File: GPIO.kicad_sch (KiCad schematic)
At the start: 7 parts, among them J9 uPD446

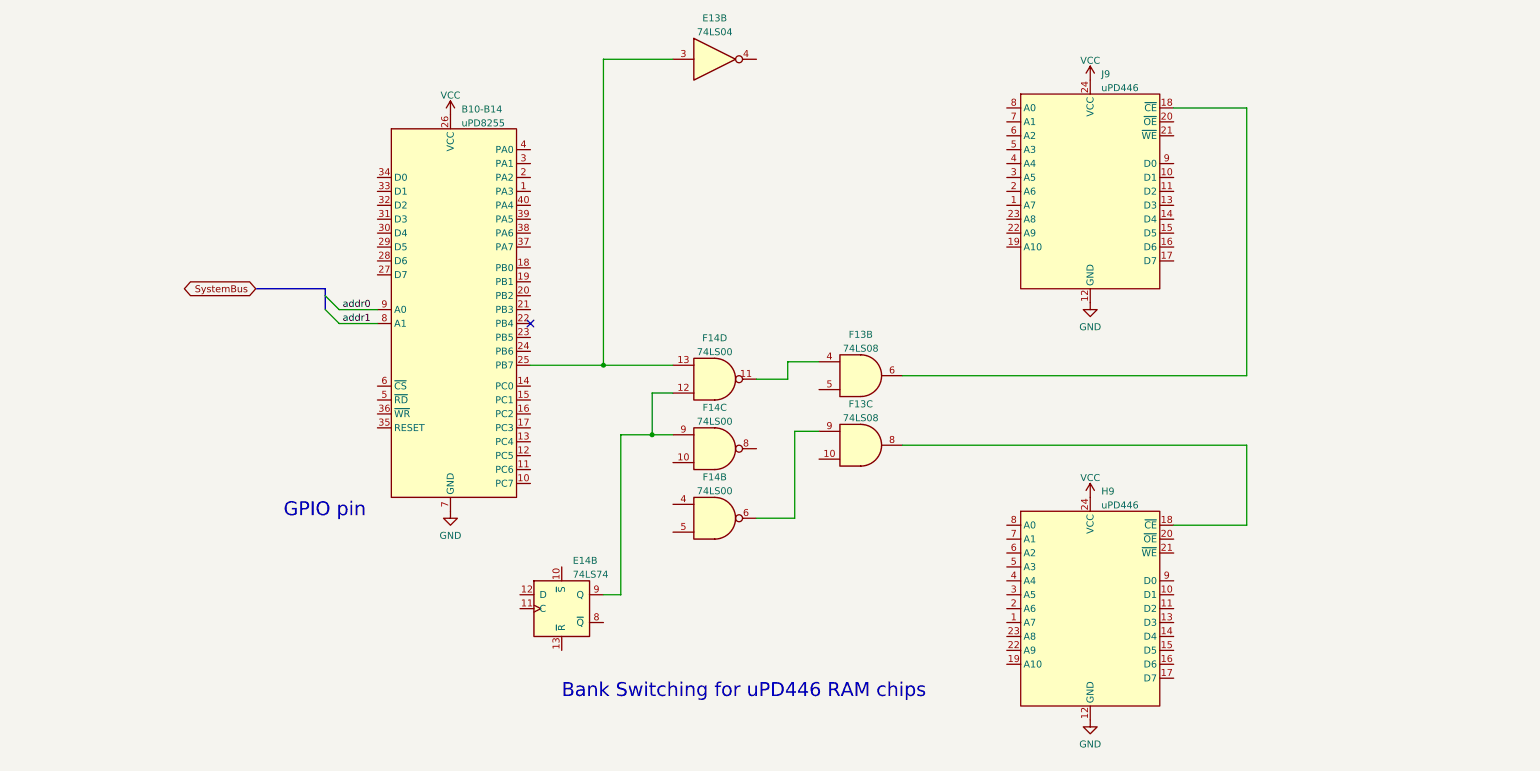
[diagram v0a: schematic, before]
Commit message: Some steps in bank switching and crtc circuits
- crtc pixel clock generator
- 2k ram, enabling logic (heavily incomplete)
- other 2k ram, annotation regarding data bus
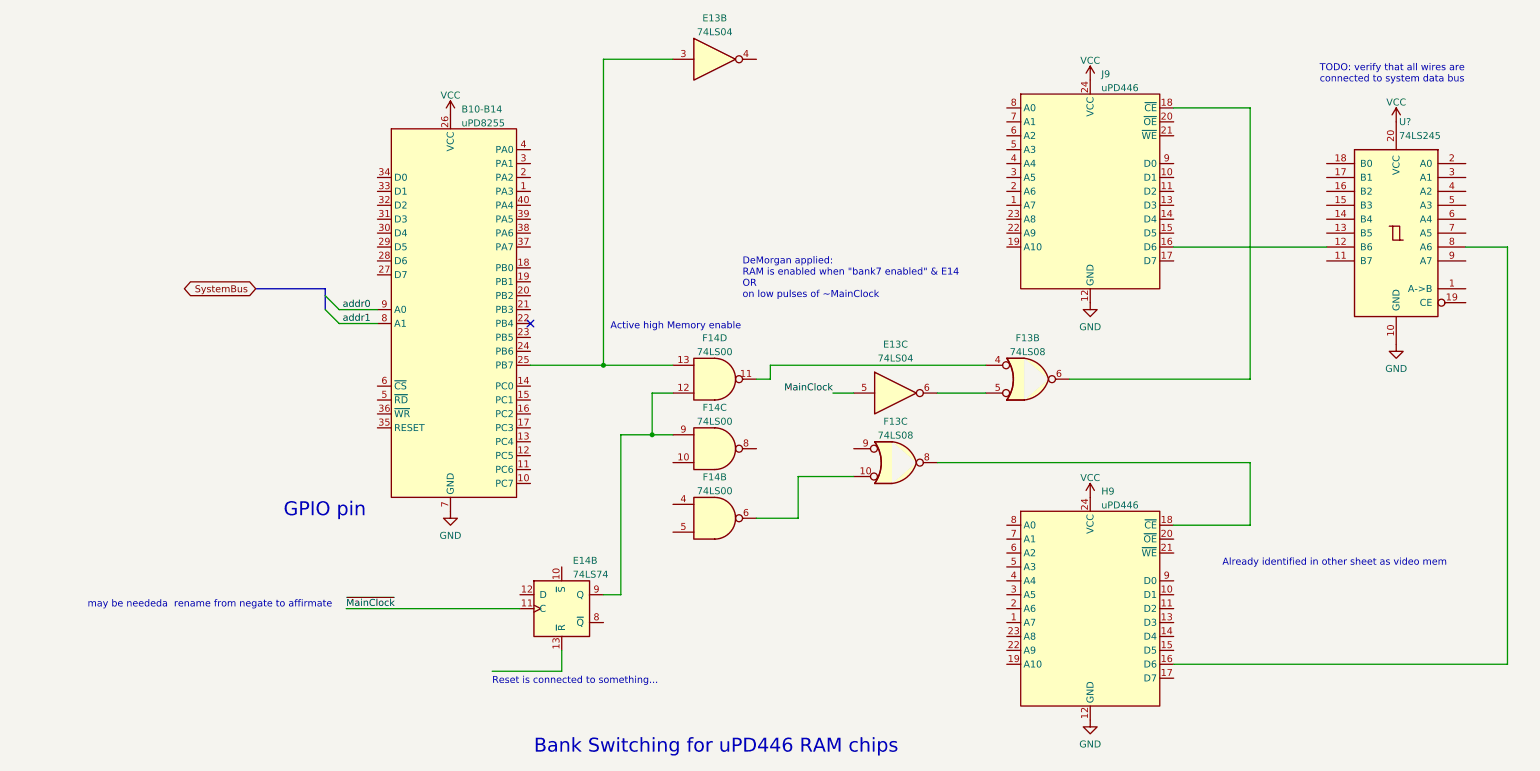
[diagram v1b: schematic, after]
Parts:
- added unit 3 of E13
- added U?: 74LS245, symbol 74xx:74LS245
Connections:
- net GND: now also U?.10 (GND)
- net VCC: now also U?.20 (VCC)
- net at F14.6: now also F13.10; no longer F13.9
- net ~{MainClock}: now reaches E14.11 (C)
- net at H9.16 (D6): now also U?.8 (A6)
- net at J9.16 (D6): now also U?.12 (B6)
- net at F13.5: now also E13.6
- new net MainClock: E13.5
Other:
- note added: "Active high Memory enable"
- note added: "Already identified in other sheet as video mem"
- note added: "DeMorgan applied: RAM is enabled when "bank7 enabled" & E14 OR on low pulses of ~MainClock"
- note added: "Reset is connected to something..."
- note added: "TODO: verify that all wires are connected to system data bus"
- note added: "may be neededa rename from negate to affirmate"

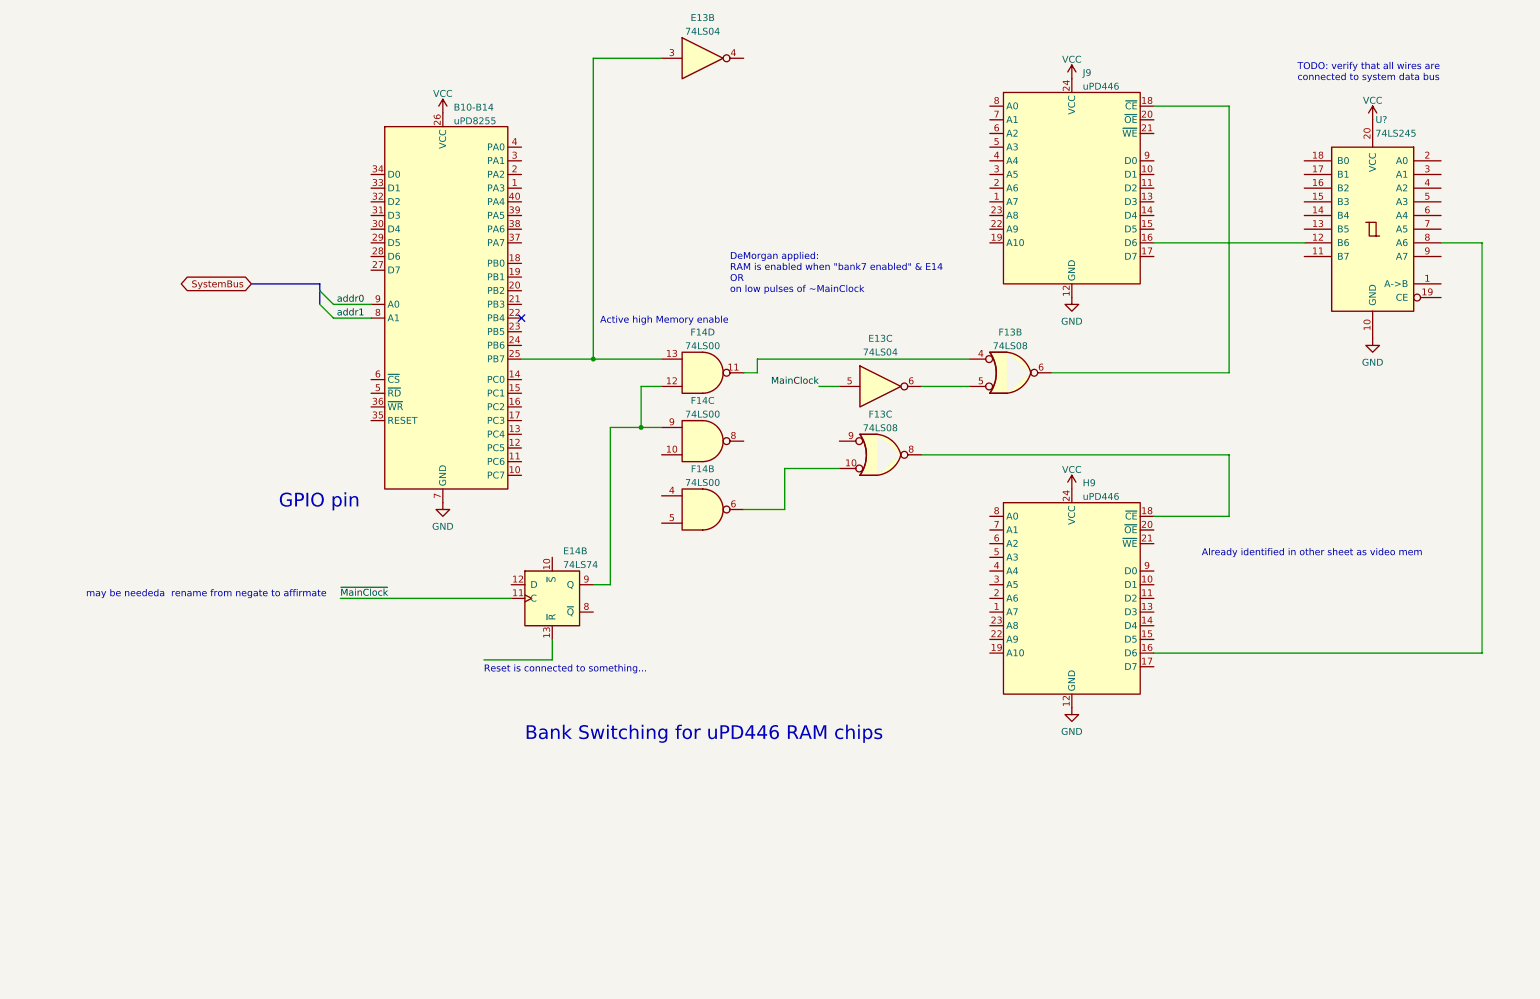
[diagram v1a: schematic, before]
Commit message: Video memory bus and connections to Z80
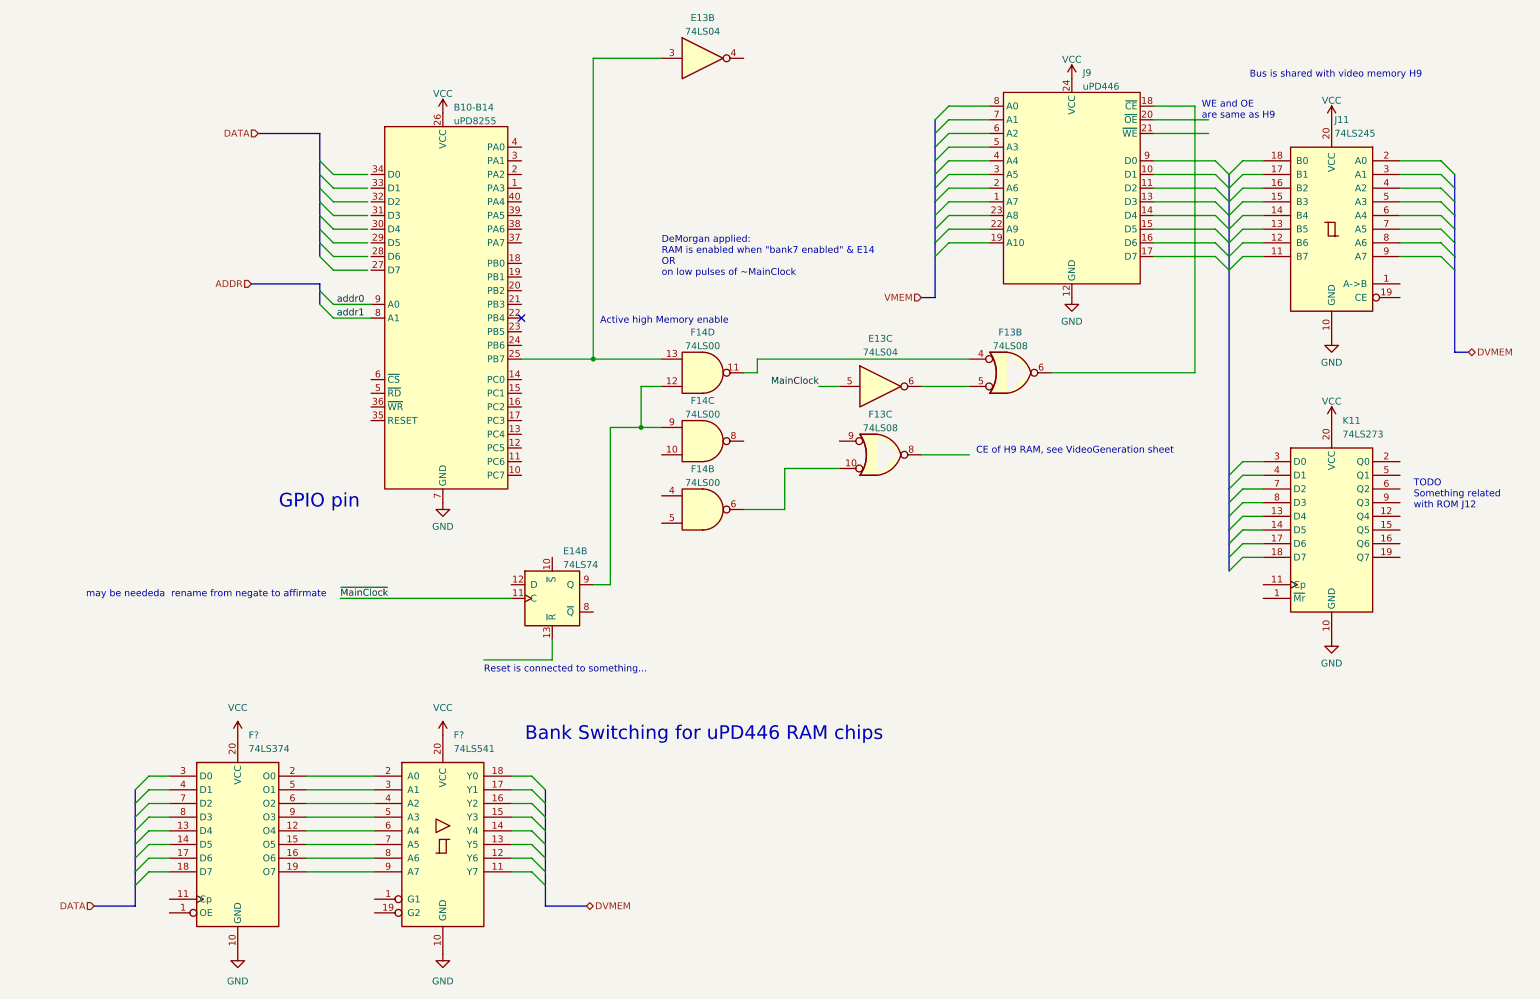
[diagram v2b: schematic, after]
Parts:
- removed H9: uPD446, symbol ceda:uPD446
- added F?: 74LS541, symbol 74xx:74LS541
- added F?: 74LS374, symbol 74xx:74LS374
- added K11: 74LS273, symbol 74xx:74LS273
- gave numbers to parts that had none: 1
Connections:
- net GND: now also F?.10 (GND), F?.10 (GND), K11.10 (GND)
- net VCC: now also F?.20 (VCC), F?.20 (VCC), K11.20 (VCC)
- net at J11.12 (B6): no longer J9.16 (D6)
- new net: F?.2 (A0), F?.2 (O0)
- new net: F?.3 (A1), F?.5 (O1)
- new net: F?.4 (A2), F?.6 (O2)
- new net: F?.5 (A3), F?.9 (O3)
- new net: F?.12 (O4), F?.6 (A4)
- new net: F?.15 (O5), F?.7 (A5)
- new net: F?.16 (O6), F?.8 (A6)
- new net: F?.19 (O7), F?.9 (A7)
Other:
- note added: "Bus is shared with video memory H9"
- note added: "CE of H9 RAM, see VideoGeneration sheet"
- note added: "TODO Something related with ROM J12"
- note added: "WE and OE are same as H9"
- note removed: "Already identified in other sheet as video mem"
- note removed: "TODO: verify that all wires are connected to system data bus"
- moved on the sheet: J11

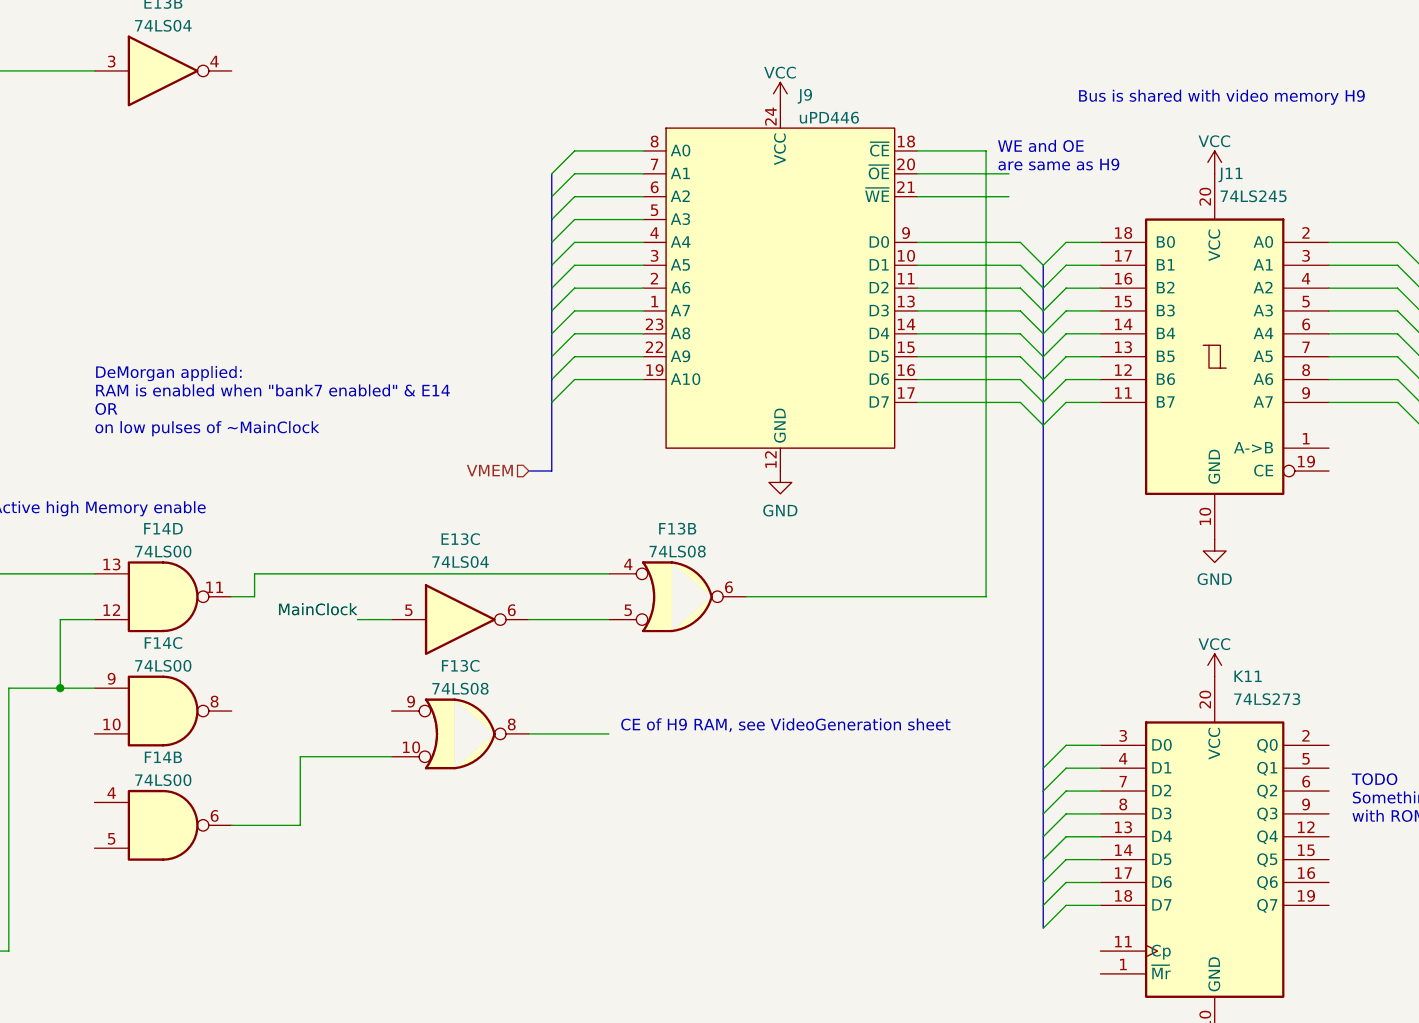
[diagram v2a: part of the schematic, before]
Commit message: Upgraded to kicad 7
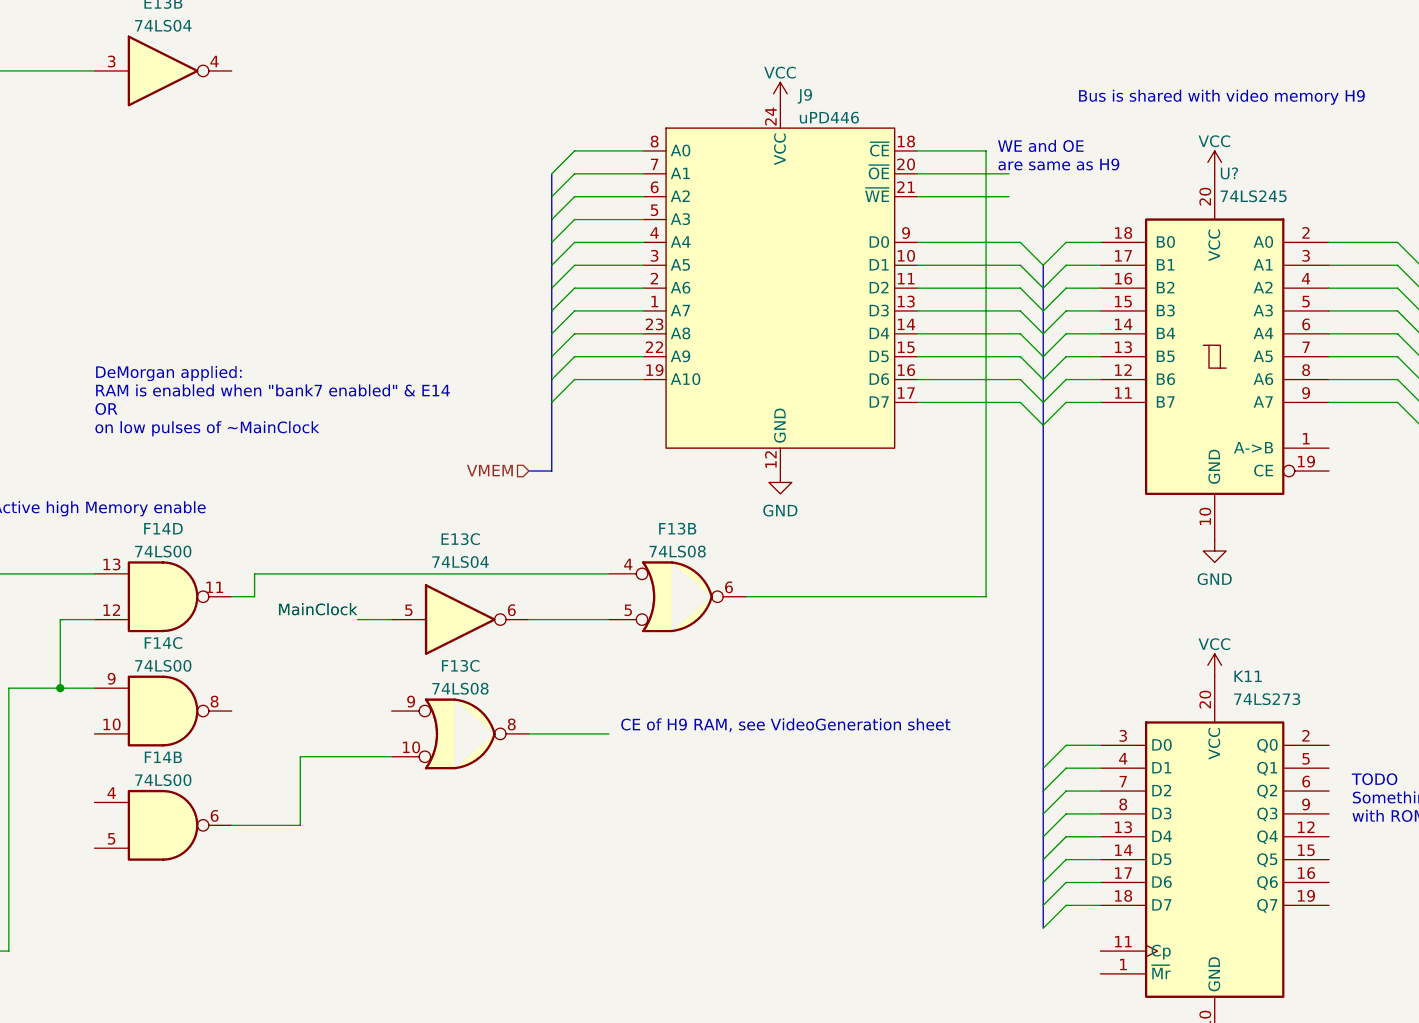
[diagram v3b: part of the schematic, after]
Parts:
- renumbered J11 to U?
